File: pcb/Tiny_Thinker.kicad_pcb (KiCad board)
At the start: 4 copper layers, 65 x 63.1 mm, 45 parts, among them J2 PERIPHERALS, J3 ADC_TIM, J8 USB_C_Receptacle_USB2.0_16P, SW1 SW_Push, SW2 SW_SPDT, U1 STM32F446RET6, U2 AMS1117-3.3, Y1 16MHz

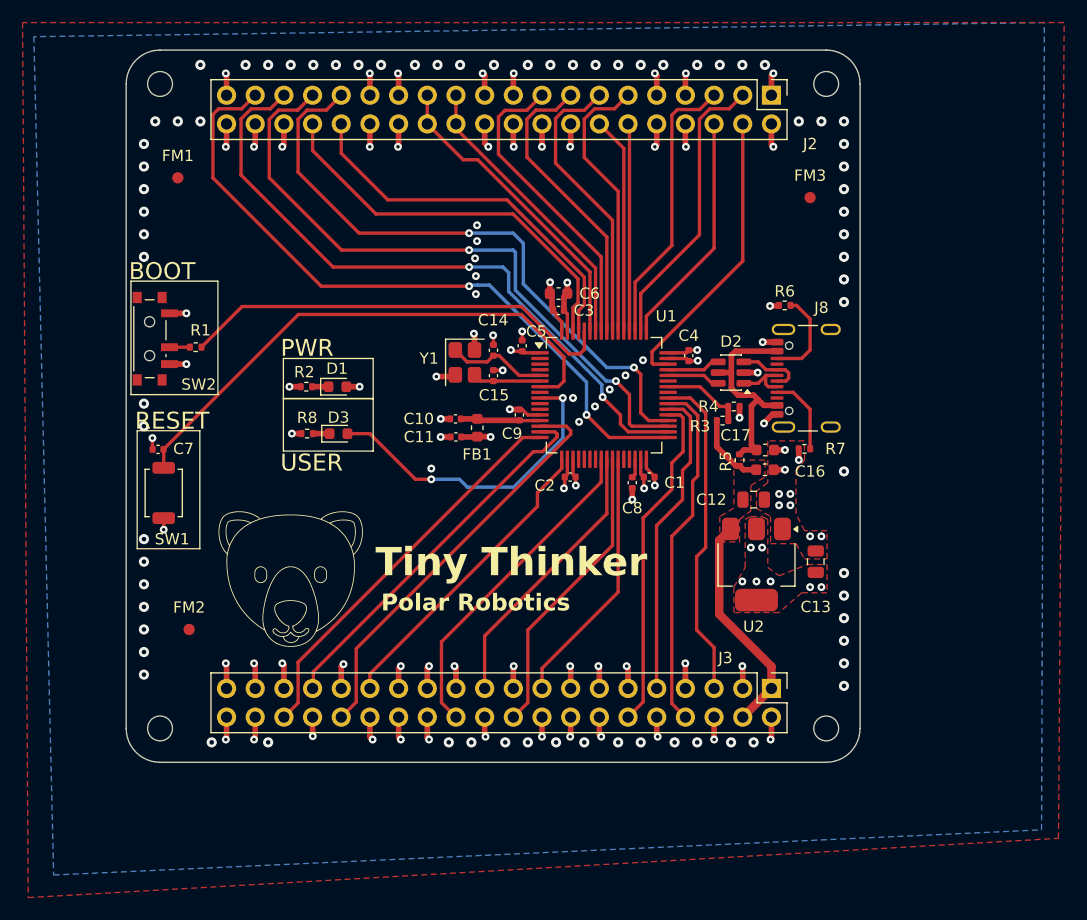
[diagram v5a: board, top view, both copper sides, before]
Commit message: changed dimensions to be whole numbers
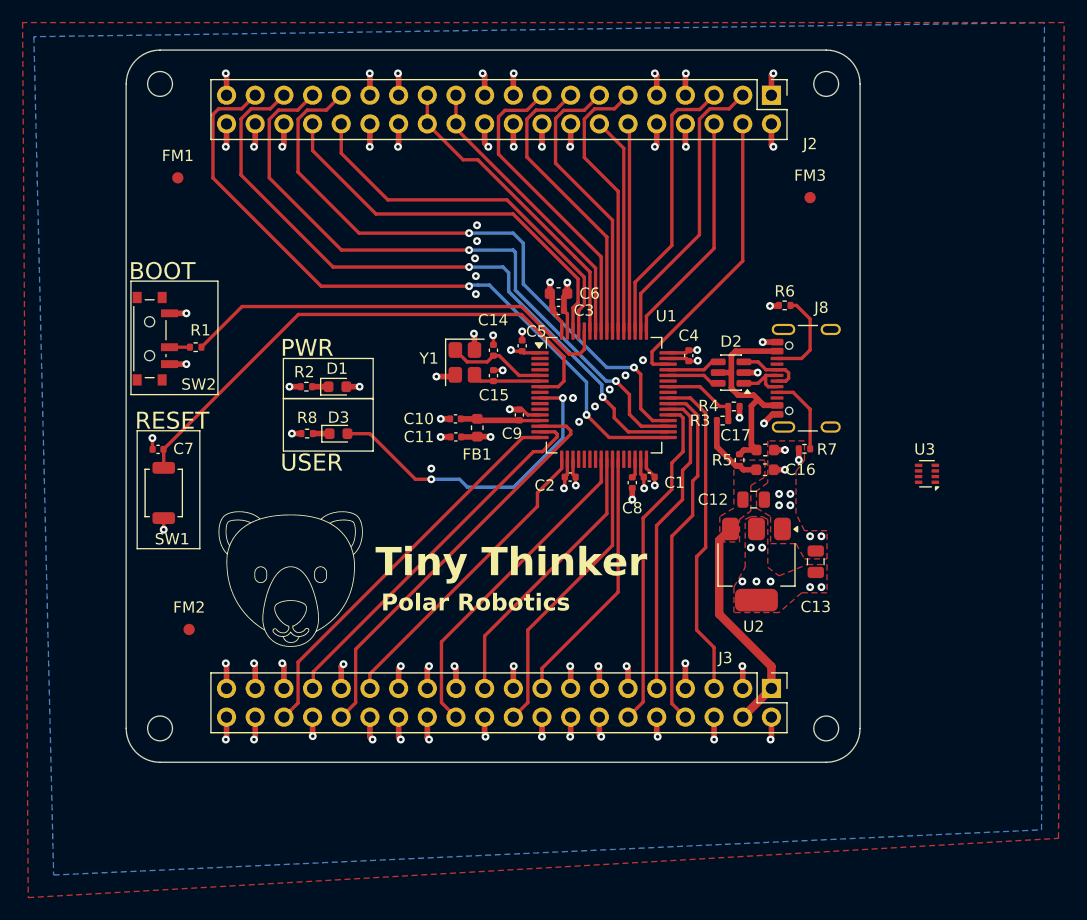
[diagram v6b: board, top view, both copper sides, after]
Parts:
- added U3: TPS2116DRL, Package_TO_SOT_SMD:SOT-583-8, F.Cu at (165.3, 108.2)
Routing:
- net GND: vias 147 -> 74

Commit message: added and routed TPS2116 Power OR-ing IC
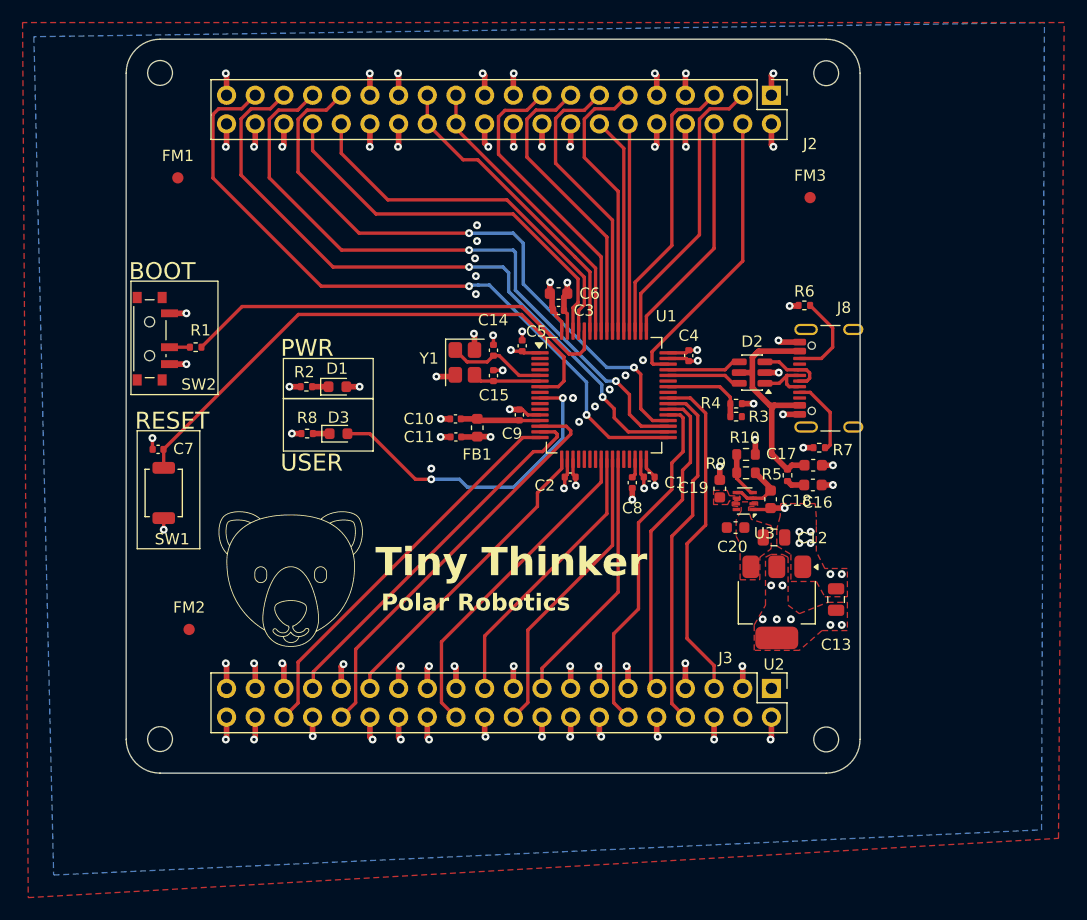
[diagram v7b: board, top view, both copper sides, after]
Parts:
- added C18: 10uF, Capacitor_SMD:C_0603_1608Metric, F.Cu at (151.5, 110.5)
- added C19: 10uF, Capacitor_SMD:C_0603_1608Metric, F.Cu at (147.0, 109.5)
- added C20: 10uF, Capacitor_SMD:C_0603_1608Metric, F.Cu at (148.4, 113.0)
- added R10: 100k, Resistor_SMD:R_0603_1608Metric, F.Cu at (149.3, 106.5)
- added R9: 100k, Resistor_SMD:R_0603_1608Metric, F.Cu at (149.3, 108.1)
- moved U3 16.3 mm to (149.2, 110.6)
- moved C16 4.46 mm to (155.2, 109.2)
- moved C17 4.46 mm to (155.3, 107.5)
- moved R5 4.46 mm to (153.0, 108.3)
- moved C12 3.80 mm to (151.8, 113.8)
- moved C13 3.80 mm to (157.3, 119.3)
- moved U2 3.80 mm to (152.1, 119.6)
- moved J8 2.00 mm to (157.8, 99.8)
- moved D2 1.86 mm to (149.9, 99.2)
- moved R6 1.74 mm to (154.5, 93.3)
- moved R7 1.31 mm to (155.8, 105.9)
- moved R3 1.25 mm to (148.4, 103.2), turned to 180 degrees
- moved H1 0.98 mm to (97.4, 72.7)
- moved H3 0.97 mm to (156.4, 131.7)
- moved H4 0.95 mm to (156.4, 72.7)
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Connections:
- net /USB__CONN_D+ renamed /USB_CONN_D+
- net /USB__CONN_D- renamed /USB_CONN_D-
- C12 pad 1: +VBUSF -> +5V_SYS
- U2 pad 3: +VBUSF -> +5V_SYS
- U3 pad 2: Net-(U3-VOUT-Pad2) -> +5V_SYS
- U3 pad 3: unconnected-(U3-VIN1-Pad3) -> +VBUSF
- U3 pad 4: unconnected-(U3-PR1-Pad4) -> /PR1
- U3 pad 5: unconnected-(U3-MODE-Pad5) -> +VBUSF
- U3 pad 6: unconnected-(U3-VIN2-Pad6) -> +5V_EXT
- U3 pad 7: Net-(U3-VOUT-Pad2) -> +5V_SYS
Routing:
- net +VBUSF: track 26.7 -> 7.34 mm
- net GND: track 99.2 -> 104.9 mm, vias 74 -> 77
- net /PR1: track 0.00 -> 4.02 mm
- net +VBUS: track 19.5 -> 21.1 mm
- net /USB_D-: track 4.73 -> 6.03 mm
- net /USB_D+: track 4.73 -> 6.03 mm
- net /TIM3_CH1: track 30.0 -> 31.0 mm
- net /TIM3_CH4: track 29.2 -> 29.9 mm
- added copper zone on F.Cu, net +5V_EXT
- added copper zone on F.Cu, net +5V_SYS
- removed copper zone on F.Cu, net +VBUSF
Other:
- board size 65 x 63.1 mm -> 65 x 65 mm
